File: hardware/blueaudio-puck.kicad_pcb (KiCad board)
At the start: 2 copper layers, 60 x 55 mm, 48 parts, among them J1 USB-C, J2 3.5mm, J3 OLED, J4 BATT, J5 PROG, Q1 MMBT3904, Q2 MMBT3904, SW1 MODE, SW2 RESET, SW3 BOOT, U1 ESP32-WROOM-32U, U2 PCM5102A, U3 MCP73831-2-OT, U4 AP2112K-3.3, U5 LP2985-3.3

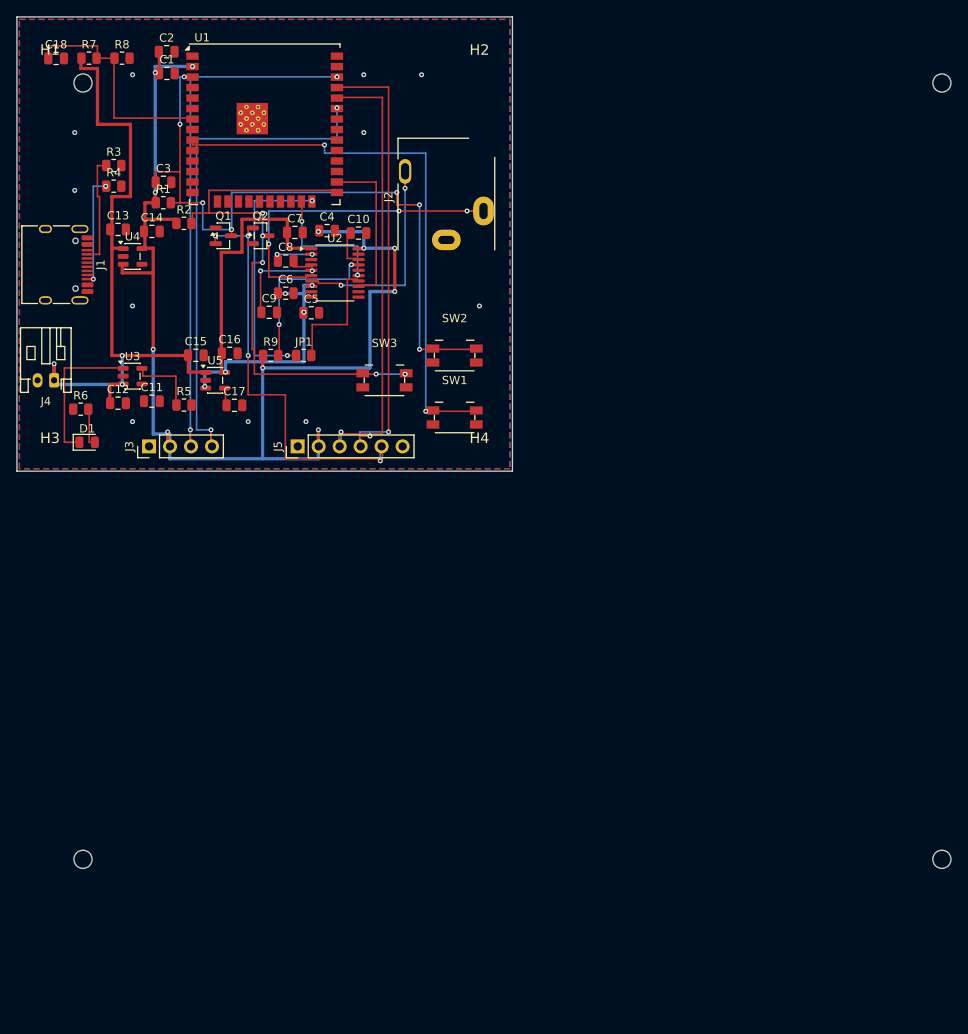
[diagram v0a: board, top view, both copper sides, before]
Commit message: hw: three user buttons, JLCPCB rules, and a router that models copper width
Brings the board in line with the three-button firmware, and fixes three
geometry bugs in the router that were producing copper which looked right and
was not.

Buttons. SW1/SW2/SW3 are now BT1/BT2/BT3 on GPIO 32/33/27, matching the
firmware; RESET and BOOT move to SW4/SW5. They sit in a row along the bottom
edge in the order a thumb expects -- previous, play, next. The board grew from
60x55 to 60x64 to make room: the old bottom edge was already full of headers,
and squeezing five switches into the sides would have put the two people press
constantly behind the headphone jack.

Worth recording: there is no LED on GPIO 27 on this board. The Kconfig help for
PUCK_LED_GPIO suggests 27 for an external status LED, which collides with BT3
on a breadboard. Here the only LED is D1 on CHG_STAT, so the pin is
unambiguously BT3.

JLCPCB rules are now in the project file, so DRC enforces them instead of
leaving them as folklore: 0.15 mm clearance, 0.2 mm track, 0.3 mm via drill,
0.13 mm annular ring, 0.5 mm hole-to-hole, 0.5 mm to the outline. Every value
sits at or inside their standard two-layer capability. Clearance is the only
one near a limit and is still 18% above their floor -- and the 0.05 mm it frees
per side against KiCad's 0.2 mm default is most of what lets the congested area
route at all. Teardrop parameters are configured too, though KiCad only
generates teardrops on demand, so they are a post-routing step rather than
something these files contain.

Three router bugs, each of which produced DRC-failing copper:

- A track is not a point. A 0.4 mm power track centred on a 0.25 mm grid cell
  spills into its neighbours, and checking only the cell it steps through let
  one sit 0.15 mm from a pad. Vias are worse: 0.6 mm across, and one landed on
  top of another net's track. Both now check every cell their copper covers.
- Clearance belongs in the check, not the map. Growing a clearance halo a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
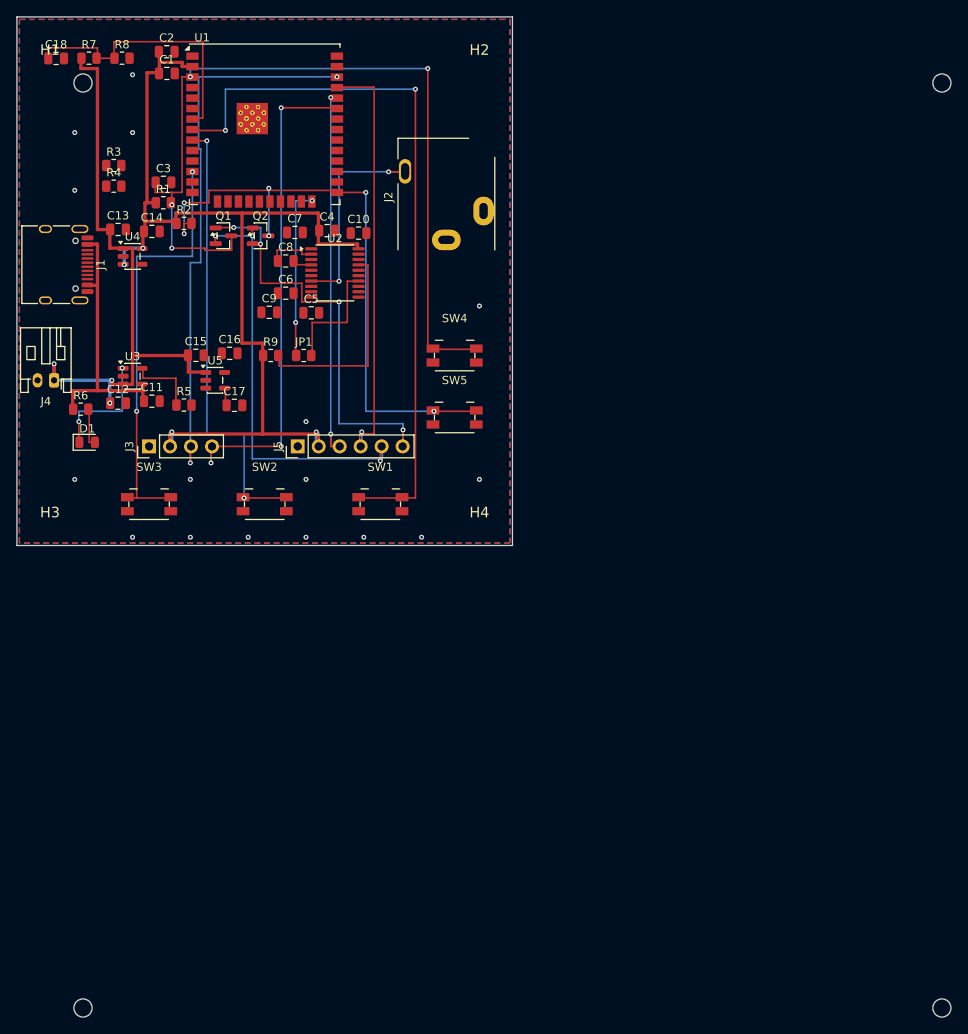
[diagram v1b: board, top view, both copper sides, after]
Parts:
- added SW4: RESET, Panasonic_EVQPUJ_EVQPUA, F.Cu at (53.0, 41.0)
- added SW5: BOOT, Panasonic_EVQPUJ_EVQPUA, F.Cu at (53.0, 48.5)
- SW1: value MODE -> BT1
- SW2: value RESET -> BT2
- SW3: value BOOT -> BT3
- moved SW3 32.2 mm to (16.0, 59.0)
- moved SW2 29.2 mm to (30.0, 59.0)
- moved SW1 13.8 mm to (44.0, 59.0)
- moved H3 9.00 mm to (4.00, 60.0)
- moved H4 9.00 mm to (56.0, 60.0)
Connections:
- SW1 pad 1: BTN_MODE -> BTN_1
- SW2 pad 1: EN -> BTN_2
- SW3 pad 1: IO0 -> BTN_3
- U1 pad 12: (no net) -> BTN_3
- U1 pad 8: (no net) -> BTN_1
- U1 pad 9: BTN_MODE -> BTN_2
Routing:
- net BTN_1: track 0.00 -> 88.2 mm, vias 0 -> 2
- net BTN_MODE: track 67.0 -> 0.00 mm, vias 2 -> 0
- net +3V3A: track 62.2 -> 0.00 mm, vias 5 -> 0
- net BTN_2: track 0.00 -> 54.5 mm, vias 0 -> 2
- net RTS: track 0.00 -> 52.2 mm, vias 0 -> 4
- net BTN_3: track 0.00 -> 51.2 mm, vias 0 -> 2
- net AUDIO_L: track 41.5 -> 0.00 mm, vias 3 -> 0
- net VBUS: track 0.00 -> 33.2 mm
- net +3V3: track 149.2 -> 121.8 mm, vias 11 -> 4
- net EN: track 85.2 -> 105.2 mm, vias 7 -> 4
- net I2S_BCK: track 19.5 -> 0.00 mm
- net I2S_LRCK: track 15.8 -> 0.00 mm, vias 2 -> 0
- net CC2: track 13.5 -> 0.00 mm, vias 2 -> 0
- net CC1: track 13.5 -> 0.00 mm
- net DAC_VNEG: track 11.2 -> 0.00 mm, vias 2 -> 0
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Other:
- board size 60 x 55 mm -> 60 x 64 mm
